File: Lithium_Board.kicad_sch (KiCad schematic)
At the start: 66 parts, among them IC1 BQ25750RRVR, IC2 TPS70933DBVR, J1 XT30PW-M, J2 XT30PW-F, J3 XT30PW-M, J5 TSW-105-07-G-S, Q1 SIR870ADP-T1-GE3, Q2 SIR870ADP-T1-GE3, Q3 SIR870ADP-T1-GE3, Q4 SIR870ADP-T1-GE3, Q5 SIR870ADP-T1-GE3, Q6 SIR870ADP-T1-GE3, Q7 SIR870ADP-T1-GE3, Q8 SIR870ADP-T1-GE3

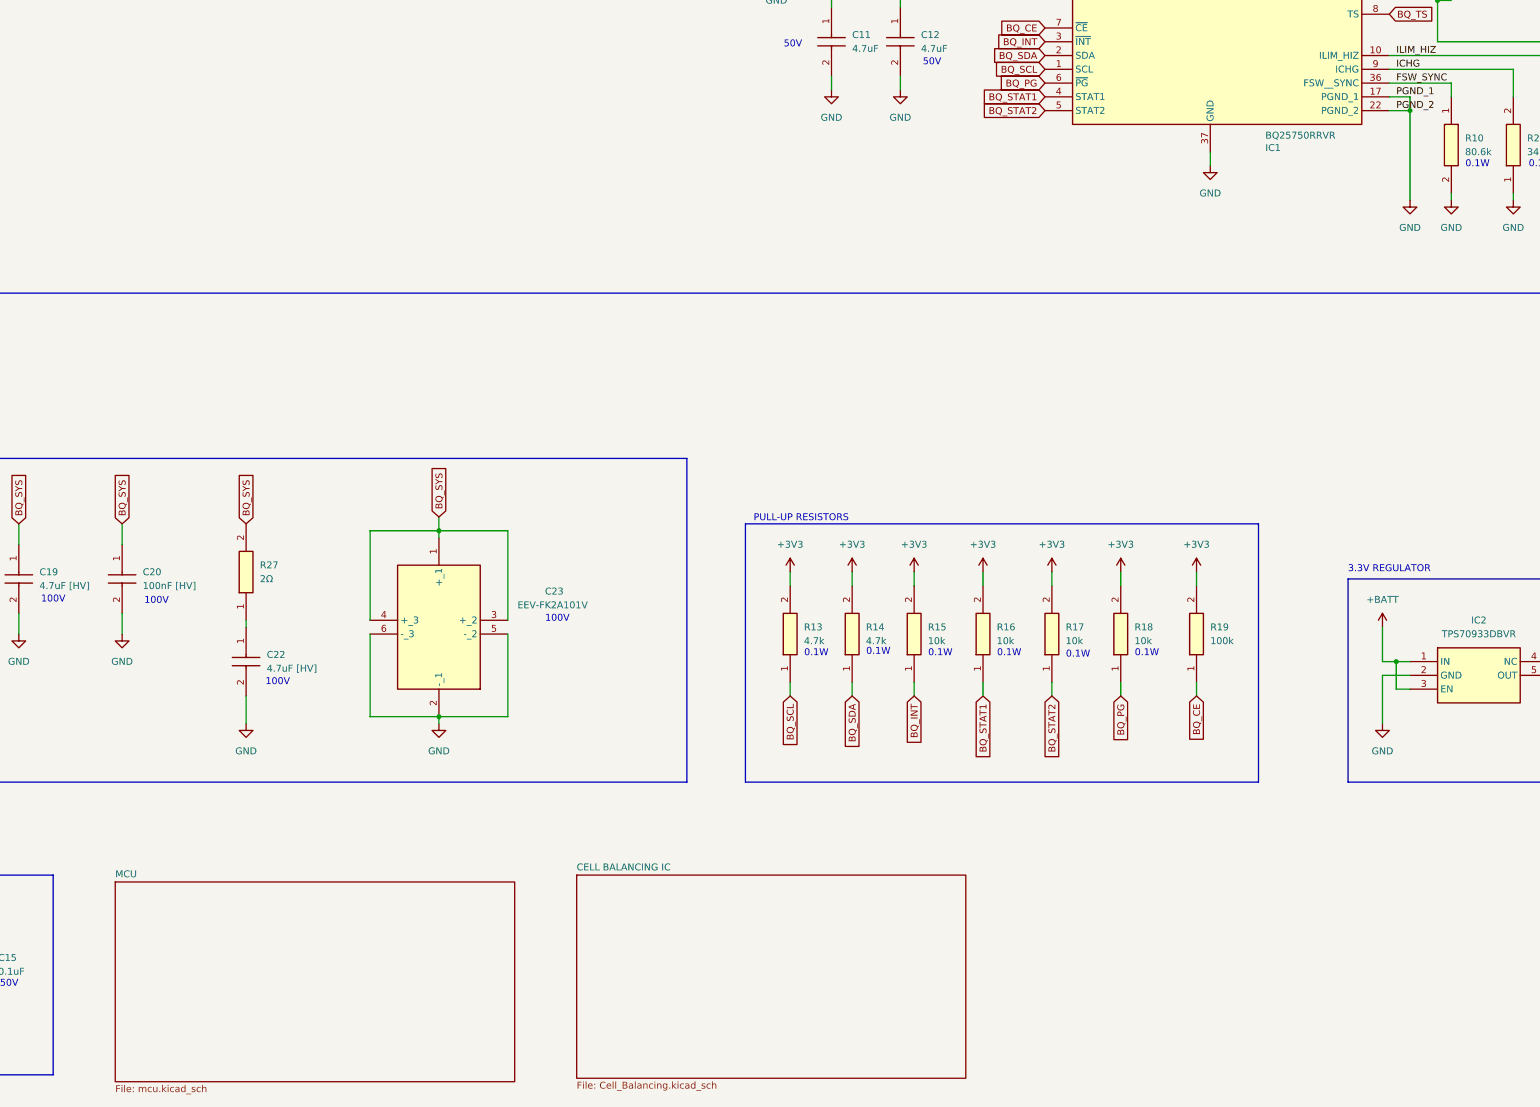
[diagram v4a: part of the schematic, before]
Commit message: Added Canbus+LEDs+New STM32
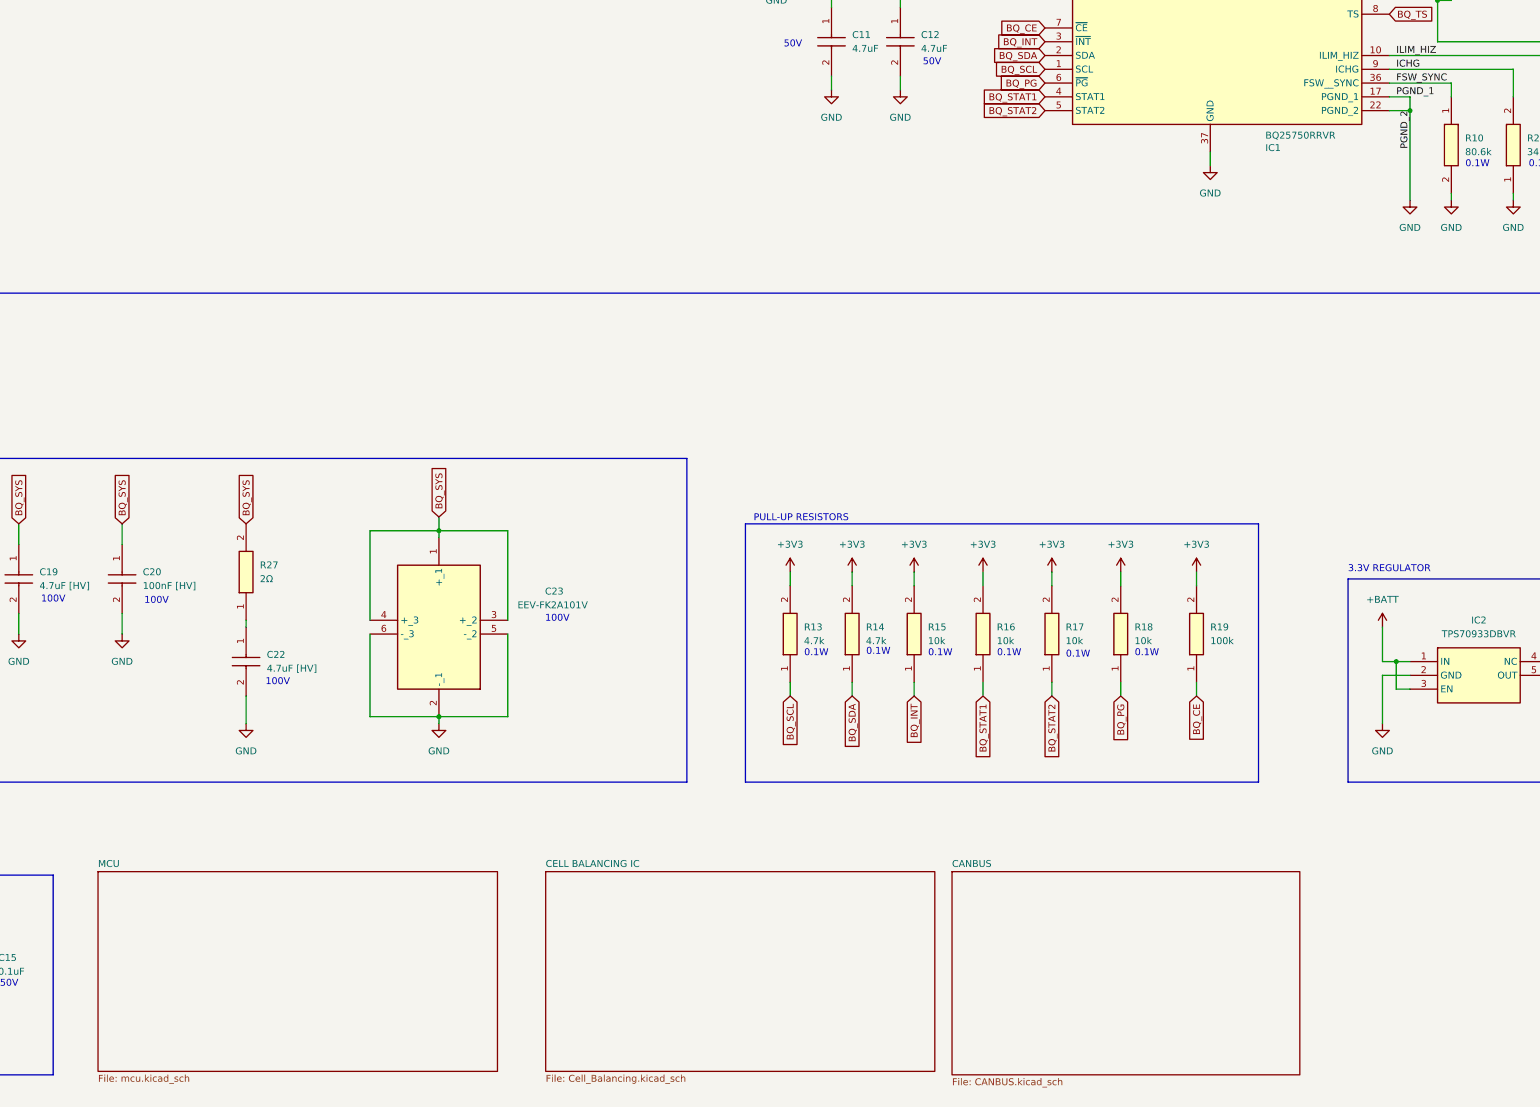
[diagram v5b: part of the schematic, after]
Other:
- added sheet CANBUS (CANBUS.kicad_sch)
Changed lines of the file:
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@@
 	(wire
 		(pts
+			(xy 353.06 168.91) (xy 356.87 168.91)
+		)
+		(stroke
+			(width 0)
+			(type default)
+		)
+	)
+	(wire
+		(pts
 			(xy 175.26 69.85) (xy 175.26 72.39)
 		)
@@
 	(wire
 		(pts
-			(xy 356.87 168.91) (xy 356.87 185.42)
+			(xy 142.24 276.86) (xy 142.24 281.94)
 		)
 		(stroke
@@
 	(wire
 		(pts
-			(xy 142.24 276.86) (xy 142.24 281.94)
+			(xy 408.94 153.67) (xy 431.8 153.67)
 		)
 		(stroke
@@
 	(wire
 		(pts
-			(xy 408.94 153.67) (xy 431.8 153.67)
+			(xy 293.37 77.47) (xy 293.37 83.82)
 		)
 		(stroke
@@
 	(wire
 		(pts
-			(xy 293.37 77.47) (xy 293.37 83.82)
+			(xy 54.61 280.67) (xy 54.61 283.21)
 		)
 		(stroke
@@
 	(wire
 		(pts
-			(xy 54.61 280.67) (xy 54.61 283.21)
+			(xy 356.87 168.91) (xy 356.87 185.42)
 		)
 		(stroke
@@
 	(wire
 		(pts
-			(xy 353.06 168.91) (xy 356.87 168.91)
-		)
-		(stroke
-			(width 0)
-			(type default)
-		)
-	)
-	(wire
-		(pts
 			(xy 353.06 137.16) (xy 367.03 137.16)
 		)
@@
 	)
 	(label "PGND_2"
-		(at 354.33 168.91 0)
+		(at 356.87 168.91 270)
 		(effects
 			(font
 				(size 1.27 1.27)
 			)
-			(justify left bottom)
+			(justify right bottom)
 		)
 	)
@@
 	)
 	(sheet
-		(at 118.11 311.15)
+		(at 114.935 309.245)
 		(size 73.66 36.83)
 		(exclude_from_sim no)
@@
 		)
 		(property "Sheetname" "MCU"
-			(at 118.11 310.4384 0)
+			(at 114.935 308.5334 0)
 			(effects
 				(font
@@
 		)
 		(property "Sheetfile" "mcu.kicad_sch"
-			(at 118.11 348.5646 0)
+			(at 114.935 346.6596 0)
 			(effects
 				(font
@@
 	)
 	(sheet
-		(at 203.2 309.88)
-		(size 71.755 37.465)
+		(at 272.415 309.245)
+		(size 64.135 37.465)
+		(exclude_from_sim no)
+		(in_bom yes)
+		(on_board yes)
+		(dnp no)
+		(fields_autoplaced yes)
+		(stroke
+			(width 0.1524)
+			(type solid)
+		)
+		(fill
+			(color 0 0 0 0.0000)
+		)
+		(property "Sheetname" "CANBUS"
+			(at 272.415 308.5334 0)
+			(effects
+				(font
+					(size 1.27 1.27)
+				)
+				(justify left bottom)
+			)
+		)
+		(property "Sheetfile" "CANBUS.kicad_sch"
+			(at 272.415 347.2946 0)
+			(effects
+				(font
+					(size 1.27 1.27)
+				)
+				(justify left top)
+			)
+		)
+		(instances
+			(project "Lithium_Board"
+				(path "/a208389b-7ee7-48d8-95f2-b3e129849547"
+					(page "4")
+				)
+			)
+		)
+	)
+	(sheet
+		(at 197.485 309.245)
+		(size 71.755 36.83)
 		(exclude_from_sim no)
 		(in_bom yes)
@@
 		)
 		(property "Sheetname" "CELL BALANCING IC"
-			(at 203.2 309.1684 0)
+			(at 197.485 308.5334 0)
 			(effects
 				(font
@@
 		)
 		(property "Sheetfile" "Cell_Balancing.kicad_sch"
-			(at 203.2 347.9296 0)
+			(at 197.485 346.6596 0)
 			(effects
 				(font

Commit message: First Layout Try
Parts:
- removed C14: 1uF, C2012X7R1H105K125AB:CAPC2012X145N, symbol C2012X7R1H105K125AB:C2012X7R1H105K125AB
- removed C15: 0.1uF, CC0603KRX7R9BB104:CAPC1608X90N, symbol CC0603KRX7R9BB104:CC0603KRX7R9BB104
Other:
- note removed: "Decoupling Capacitors"

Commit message: First Changes
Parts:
- removed C17: 1uF, C2012X7R1H105K125AB:CAPC2012X145N, symbol C2012X7R1H105K125AB:C2012X7R1H105K125AB
- removed C4, C5: 56nF, C0603C563K5RACTU:C0603, symbol C0603C563K5RACTU:C0603C563K5RACTU
- added C17: 4.7uF, UMJ325AB7475KMHP:CAPC3225X280N, symbol UMJ325AB7475KMHP:UMJ325AB7475KMHP
- added C4, C5: 0.1uF, CC0603KRX7R9BB104:CAPC1608X90N, symbol CC0603KRX7R9BB104:CC0603KRX7R9BB104
- added D2, D5: CDBMT2100-HF, SODFL3516X100N, symbol CDBMT2100-HF:CDBMT2100-HF
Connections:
- net +3V3: now also C17.1
- net +BATT: no longer IC2.3 (EN)
- net BQ_REGN: now also D2.2 (A), D5.2 (A)
- net BTST1: now also C4.1, D2.1 (K)
- net BTST2: now also C5.1, D5.1 (K)
- net GND: now also C17.2
- net SW1: now also C4.2
- net SW2: now also C5.2
- no-connect marks 7 -> 8
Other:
- note added: "DIODES"
- moved on the sheet: C11, C12

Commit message: Final PERFECT design before big changes
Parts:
- removed R24: 10k, RC0603FR-0710KL:RESC1608X55N, symbol RC0603FR-0710KL:RC0603FR-0710KL
- added R24: 1k, RC0603FR-071KL:RESC1608X55N, symbol RC0603FR-071KL:RC0603FR-071KL
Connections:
- net GND: now also R24.1
- net ILIM_HIZ: now also R24.2
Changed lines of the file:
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@@
-	)
-	(symbol
-		(lib_id "RC0603FR-0710KL:RC0603FR-0710KL")
-		(at 387.35 184.15 90)
-		(unit 1)
-		(exclude_from_sim no)
-		(in_bom yes)
-		(on_board yes)
-		(dnp no)
-		(fields_autoplaced yes)
-		(property "Reference" "R24"
-			(at 389.89 173.9899 90)
-			(effects
-				(font
-					(size 1.27 1.27)
-				)
-				(justify right)
-			)
-		)
-		(property "Value" "10k"
-			(at 389.89 176.5299 90)
-			(effects
-				(font
-					(size 1.27 1.27)
-				)
-				(justify right)
-			)
-		)
-		(property "Footprint" "RC0603FR-0710KL:RESC1608X55N"
-			(at 483.54 170.18 0)
-			(effects
-				(font
-					(size 1.27 1.27)
-				)
-				(justify left top)
-				(hide yes)
-			)
-		)
-		(property "Datasheet" "http://www.yageo.com/documents/recent/PYu-RC0603_51_RoHS_L_v5.pdf"
-			(at 583.54 170.18 0)
-			(effects
-				(font
-					(size 1.27 1.27)
-				)
-				(justify left top)
-				(hide yes)
-			)
-		)
-		(property "Description" "Yageo RC Series Thick Film Surface Mount Resistor 0603 Case 10k"
-			(at 387.35 184.15 0)
-			(effects
-				(font
-					(size 1.27 1.27)
-				)
-				(hide yes)
-			)
-		)
-		(property "Height" "0.55"
-			(at 783.54 170.18 0)
-			(effects
-				(font
-					(size 1.27 1.27)
-				)
-				(justify left top)
-				(hide yes)
-			)
-		)
-		(property "Mouser Part Number" "603-RC0603FR-0710KL"
-			(at 883.54 170.18 0)
-			(effects
-				(font
-					(size 1.27 1.27)
-				)
-				(justify left top)
-				(hide yes)
-			)
-		)
-		(property "Mouser Price/Stock" "https://www.mouser.co.uk/ProductDetail/YAGEO/RC0603FR-0710KL?qs=grNVn54RoB%252B3GtjbJj3wJQ%3D%3D"
-			(at 983.54 170.18 0)
-			(effects
-				(font
-					(size 1.27 1.27)
-				)
-				(justify left top)
-				(hide yes)
-			)
-		)
-		(property "Manufacturer_Name" "Yageo Group"
-			(at 1083.54 170.18 0)
-			(effects
-				(font
-					(size 1.27 1.27)
-				)
-				(justify left top)
-				(hide yes)
-			)
-		)
-		(property "Manufacturer_Part_Number" "RC0603FR-0710KL"
-			(at 1183.54 170.18 0)
-			(effects
-				(font
-					(size 1.27 1.27)
-				)
-				(justify left top)
-				(hide yes)
-			)
-		)
-		(pin "1"
-		)
-		(pin "2"
-		)
-		(instances
-			(project "Lithium_Board"
-				(path "/a208389b-7ee7-48d8-95f2-b3e129849547"
-					(reference "R24")
-					(unit 1)
-				)
-			)
-		)
 	)
 	(symbol
@@
 					(unit 1)
 				)
+			)
+		)
+	)
+	(symbol
+		(lib_id "RC0603FR-071KL:RC0603FR-071KL")
+		(at 387.35 184.15 90)
+		(unit 1)
+		(exclude_from_sim no)
+		(in_bom yes)
+		(on_board yes)
+		(dnp no)
+		(fields_autoplaced yes)
+		(property "Reference" "R24"
+			(at 389.89 173.9899 90)
+			(effects
+				(font
+					(size 1.27 1.27)
+				)
+				(justify right)
+			)
+		)
+		(property "Value" "1k"
+			(at 389.89 176.5299 90)
+			(effects
+				(font
+					(size 1.27 1.27)
+				)
+				(justify right)
+			)
+		)
+		(property "Footprint" "RC0603FR-071KL:RESC1608X55N"
+			(at 483.54 170.18 0)
+			(effects
+				(font
+					(size 1.27 1.27)
+				)
+				(justify left top)
+				(hide yes)
+			)
+		)
+		(property "Datasheet" "https://www.yageo.com/upload/media/product/productsearch/datasheet/rchip/PYu-RC_Group_51_RoHS_L_12.pdf"
+			(at 583.54 170.18 0)
+			(effects
+				(font
+					(size 1.27 1.27)
+				)
+				(justify left top)
+				(hide yes)
+			)
+		)
+		(property "Description" "Res Thick Film 0603 1K Ohm 1% 0.1W(1/10W) +/-100ppm/C Epoxy Pad SMD T/R"
+			(at 387.35 184.15 0)
+			(effects
+				(font
+					(size 1.27 1.27)
+				)
+				(hide yes)
+			)
+		)
+		(property "Height" "0.55"
+			(at 783.54 170.18 0)
+			(effects
+				(font
+					(size 1.27 1.27)
+				)
+				(justify left top)
+				(hide yes)
+			)
+		)
+		(property "Mouser Part Number" "603-RC0603FR-071KL"
+			(at 883.54 170.18 0)
+			(effects
+				(font
+					(size 1.27 1.27)
+				)
+				(justify left top)
+				(hide yes)
+			)
+		)
+		(property "Mouser Price/Stock" "https://www.mouser.co.uk/ProductDetail/YAGEO/RC0603FR-071KL?qs=VU8sRB4EgwApHsk4rF%2F3zg%3D%3D"
+			(at 983.54 170.18 0)
+			(effects
+				(font
+					(size 1.27 1.27)
+				)
+				(justify left top)
+				(hide yes)
+			)
+		)
+		(property "Manufacturer_Name" "Yageo Group"
+			(at 1083.54 170.18 0)
+			(effects
+				(font
+					(size 1.27 1.27)
+				)
+				(justify left top)
+				(hide yes)
+			)
+		)
+		(property "Manufacturer_Part_Number" "RC0603FR-071KL"
+			(at 1183.54 170.18 0)
+			(effects
+				(font
+					(size 1.27 1.27)
+				)
+				(justify left top)
+				(hide yes)
+			)
+		)
+		(pin "1"
+		)
+		(pin "2"
+		)
+		(instances
+			(project "Lithium_Board"
+				(path "/a208389b-7ee7-48d8-95f2-b3e129849547"
+					(reference "R24")
+					(unit 1)
+				)
